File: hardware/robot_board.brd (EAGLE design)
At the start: 95.2 x 76.1 mm, 152 parts, among them J1 POWER_JACKPTH, Q1 DMP2035U, Q2 DMP2035U, Q3 DMP2035U-7, Q4 DMP2035U-7, U1 FT232RL-BASICSSOP, U10 DRV8839, U11 LM393, U12 LM393, U16 LM393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

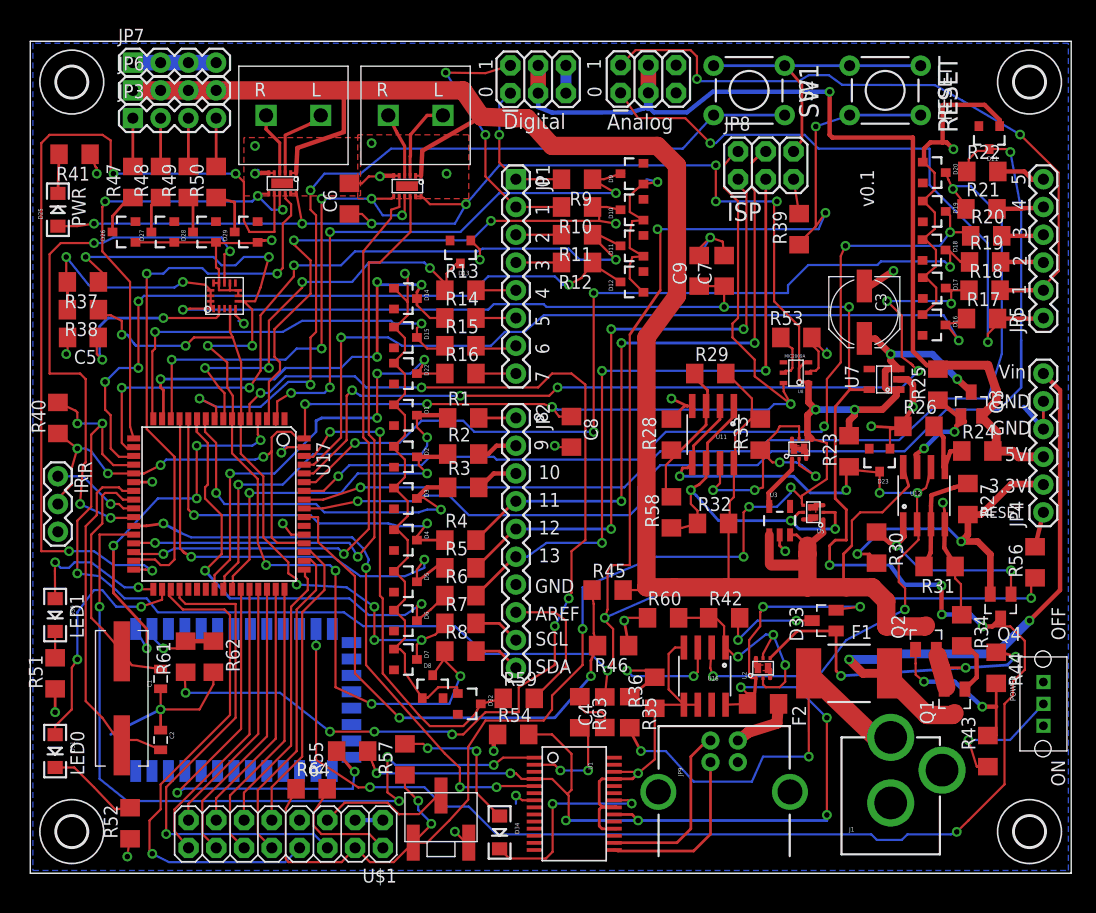
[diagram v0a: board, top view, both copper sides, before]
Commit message: fix servo bug
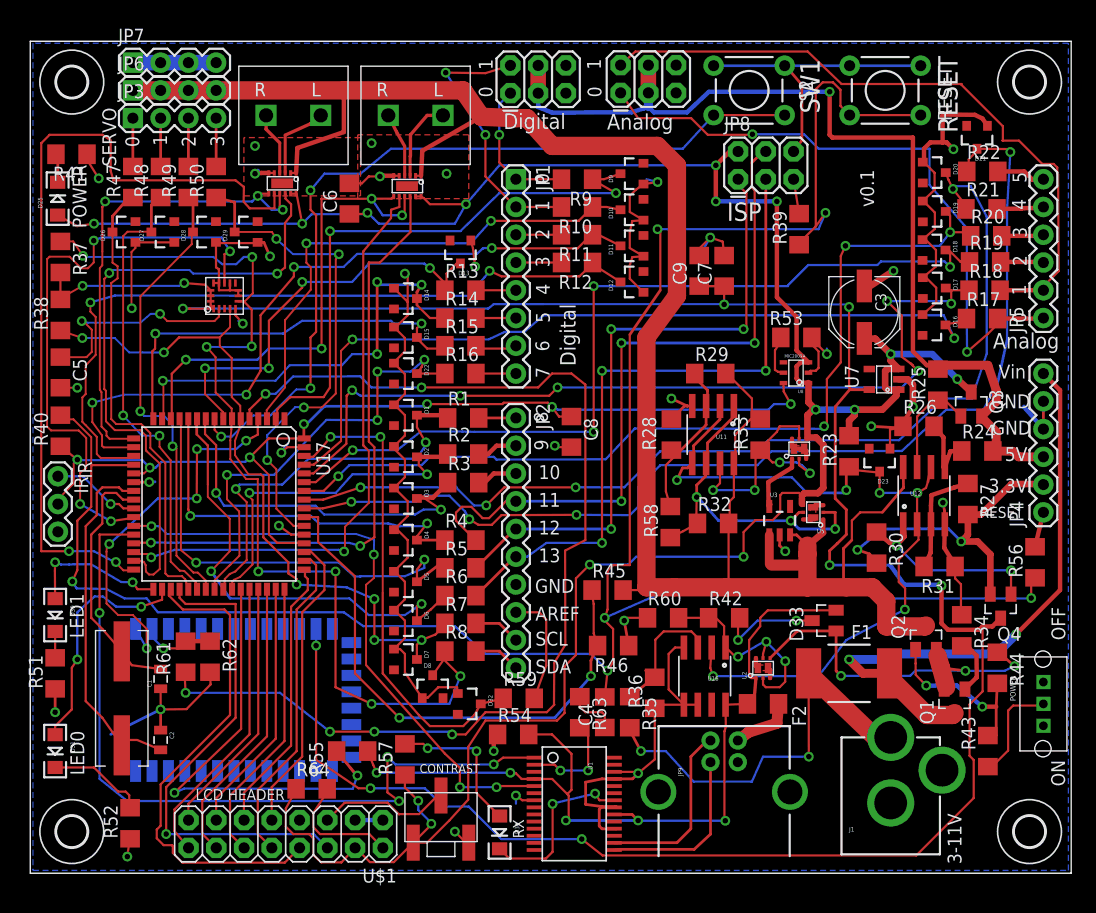
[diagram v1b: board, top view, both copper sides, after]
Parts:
- moved C5 3.80 mm to (2.77, 45.8), turned to 270 degrees
- moved R37 3.08 mm to (2.77, 56.4), turned to 270 degrees
- moved R38 2.11 mm to (2.77, 51.1), turned to 90 degrees
- moved R40 1.19 mm to (2.77, 40.5)
- moved D21 1.12 mm to (86.6, 67.4)
- moved D25 1.02 mm to (2.51, 61.7)
- moved R58 0.89 mm to (58.6, 32.1)
- moved R3 0.43 mm to (39.6, 35.7)
- moved R62 0.30 mm to (16.5, 19.8)
- moved R41 0.28 mm to (3.78, 65.8)
- moved R44 0.10 mm to (88.5, 18.8)
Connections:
- net 5V: now also JP8.2
- net 5V_UC: no longer JP8.2
- net GND: now also U4.21
- net SERVO0_IN: now also U17.37
- net SERVO1_IN: now also U17.38
- net SERVO2_IN: now also U17.39
- net SERVO3_IN: now also U17.54
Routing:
- net SERVO3_IN: track 4.47 -> 45.9 mm, vias 0 -> 4
- net SERVO1_IN: track 3.80 -> 42.7 mm, vias 0 -> 2
- net SERVO2_IN: track 3.63 -> 42.1 mm, vias 0 -> 2
- net SERVO0_IN: track 4.31 -> 42.5 mm
- net 5V_UC: track 122.4 -> 93.6 mm, vias 8 -> 7
- net USB_5V: track 101.1 -> 77.6 mm, vias 9 -> 5
- net 3V3: track 237.3 -> 228.4 mm, vias 12 -> 10
- net M1_DIR1: track 82.5 -> 74.9 mm, vias 4 -> 2
- net M1_DIR0: track 51.8 -> 58.0 mm
- net D1_IN: track 53.2 -> 47.9 mm, vias 3 -> 2
- net D11: track 59.8 -> 64.8 mm
- net D3_IN: track 65.7 -> 70.2 mm, vias 4 -> 2
- net 5V: track 235.7 -> 239.3 mm, vias 17 -> 15
- net N$8: track 17.4 -> 20.4 mm
- net N$10: track 18.8 -> 15.9 mm
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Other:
- board text added: "3-11V"
- board text added: "CONTRAST"
- board text added: "LCD HEADER"
- board text added: "POWER"
- board text added: "RX"
- board text added: "SERVO"
- board text removed: "PWR"
